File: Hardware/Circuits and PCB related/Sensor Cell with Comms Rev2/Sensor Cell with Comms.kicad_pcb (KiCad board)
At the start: 4 copper layers, 70 x 77 mm, 92 parts, among them J1 MolexMicroFit3_1, J2 MolexMicroFit3_2, J3 MolexMicroFit3_3, U1 STM32F103C6T6, U10 TPS22950x, U11 TPS2421, U2 FM24V05, U3 TMP75B, U4 TMP75B, U5 TMP75B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

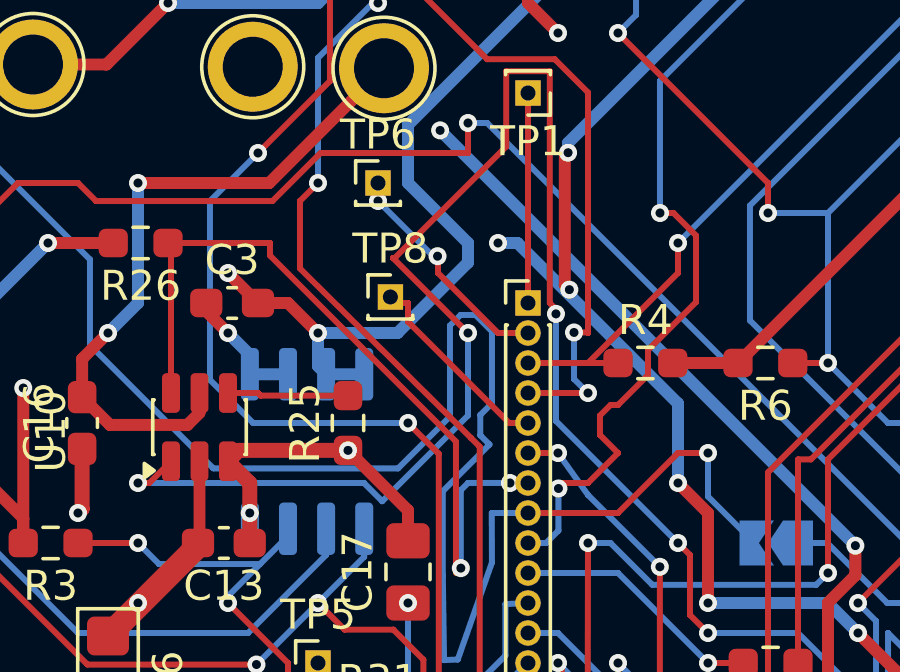
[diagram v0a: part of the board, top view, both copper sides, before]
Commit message: Found a GUI driven code tool, lets me configure every pin via a GUI and now we just need to write the logical steps of what signals do what. Need to Re-add the MCP2518 open source driver since I deleted the entire old code for my STM as it kept bringing errors due to my misconfigurations
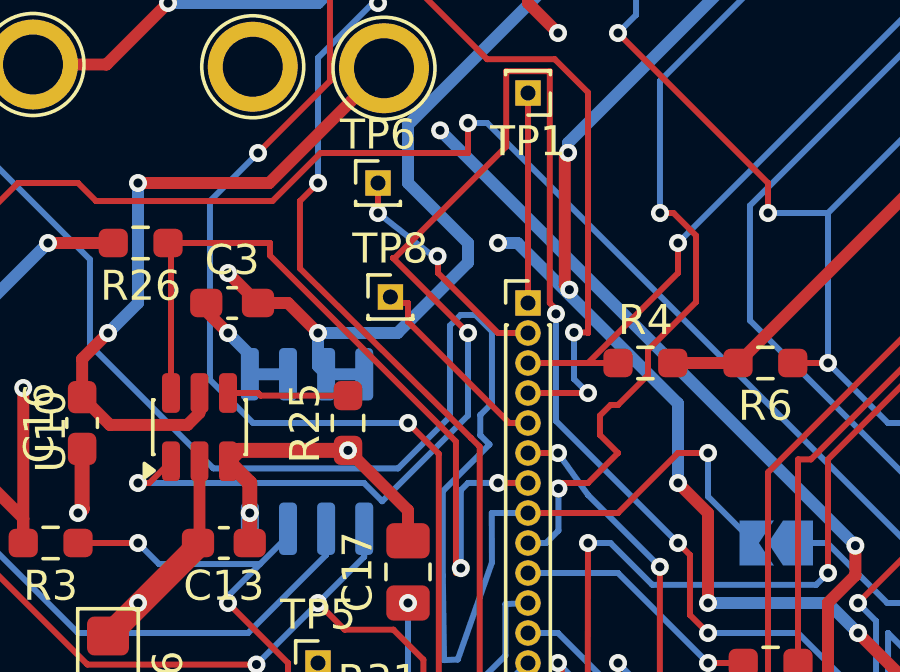
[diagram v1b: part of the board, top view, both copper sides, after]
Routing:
- net /1V8_~{FLT}: track 26.9 -> 27.7 mm
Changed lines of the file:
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@@
 		)
 		(property "Value" "RCLAMP01811PW.C"
-			(at 2.55 4 -90)
+			(at 2.55 4 270)
 			(layer "B.Fab")
 			(effects
@@
 	)
 	(segment
-		(start 95 83)
-		(end 94.39896 83)
-		(width 0.2)
-		(layer "F.Cu")
-		(net 49)
-	)
-	(segment
 		(start 86.39896 75)
 		(end 83 75)
@@
 	)
 	(segment
+		(start 95 83)
+		(end 94 82.998)
+		(width 0.2)
+		(layer "F.Cu")
+		(net 49)
+	)
+	(segment
 		(start 83.1 75.1)
 		(end 83 75)
@@
 	)
 	(via
-		(at 94.39896 83)
+		(at 94 82.998)
 		(size 0.6)
 		(drill 0.3)
@@
 	)
 	(segment
-		(start 94.39896 83)
-		(end 94.39696 82.998)
+		(start 93.002 82.998)
+		(end 92.761399 83.238601)
 		(width 0.2)
 		(layer "B.Cu")
@@
 	)
 	(segment
-		(start 94.39696 82.998)
-		(end 93.002 82.998)
+		(start 94 82.998)
+		(end 94.39696 82.998)
 		(width 0.2)
 		(layer "B.Cu")
@@
 	)
 	(segment
-		(start 92.761399 83.238601)
-		(end 92.761399 85.83807)
+		(start 94.39696 82.998)
+		(end 93.002 82.998)
 		(width 0.2)
 		(layer "B.Cu")
@@
 	)
 	(segment
-		(start 93.002 82.998)
-		(end 92.761399 83.238601)
+		(start 92.761399 83.238601)
+		(end 92.761399 85.83807)
 		(width 0.2)
 		(layer "B.Cu")
@@
 	(segment
 		(start 90 73)
-		(end 90 73.60104)
+		(end 90 74)
 		(width 0.2)
 		(layer "F.Cu")
@@
 	)
 	(via
-		(at 90 73.60104)
+		(at 90 74)
 		(size 0.6)
 		(drill 0.3)
@@
 	)
 	(segment
-		(start 91.838663 75.439703)
-		(end 90 73.60104)
+		(start 90 74)
+		(end 91.838663 75.439703)
 		(width 0.2)
 		(layer "B.Cu")
@@
 	)
 	(segment
-		(start 91.984843 75.439703)
-		(end 91.838663 75.439703)
+		(start 91.838663 75.439703)
+		(end 91.984843 75.439703)
 		(width 0.2)
 		(layer "B.Cu")
